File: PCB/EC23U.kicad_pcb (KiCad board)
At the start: 2 copper layers, 77.2 x 137.6 mm, 77 parts, among them J1 JST, SW1 BOOT0, SW10 EC_SW, SW11 EC_SW, SW12 EC_SW, SW13 EC_SW, SW14 EC_SW, SW15 EC_SW, SW16 EC_SW, SW17 EC_SW, SW18 EC_SW, SW19 EC_SW, SW2 EC_SW, SW20 EC_SW, SW21 EC_SW, SW22 EC_SW, SW23 EC_SW, SW24 EC_SW, SW25 EC_SW, SW26 EC_SW, SW27 EC_SW, SW28 EC_SW, SW3 EC_SW, SW4 EC_SW, SW5 EC_SW, SW6 EC_SW, SW7 EC_SW, SW8 EC_SW, SW9 EC_SW, U1 STM32F401CBUx, U2 XC6206PxxxMR, U3 74HC4051, U4 OPA350, Y1 8 MHz

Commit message: WIP
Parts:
- added J2: RGB, Connector_PinSocket_2.00mm:PinSocket_1x03_P2.00mm_Vertical, F.Cu at (140.5, 43.2)
- added U5: SN74AHCT1G125, Package_TO_SOT_SMD:SOT-23-5, B.Cu at (134.0, 43.9)
- moved Y1 51.5 mm to (109.9, 48.5), turned to 180 degrees
- moved C4 48.8 mm to (105.7, 44.4), turned to 90 degrees
- moved R6 48.5 mm to (107.0, 51.8)
- moved C1 48.5 mm to (100.0, 54.8)
- moved C7 48.5 mm to (104.6, 44.4)
- moved R8 48.5 mm to (101.1, 54.9)
- moved U1 48.5 mm to (101.8, 49.6)
- moved C6 48.5 mm to (96.6, 46.9)
- moved R3 48.5 mm to (96.6, 49.9)
- moved C5 48.5 mm to (98.9, 54.8)
- moved R7 48.2 mm to (103.1, 44.8), turned to 0 degrees
- moved SW1 47.8 mm to (99.1, 43.9), turned to -90 degrees
- moved C8 47.6 mm to (109.7, 51.2)
- moved C9 47.6 mm to (109.7, 52.3)
- moved R5 44.9 mm to (96.6, 53.0)
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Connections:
- D1 pad 2: D+ -> D-
- D1 pad 3: D- -> D+
- R1 pad 2: unconnected-(R1-Pad2) -> Net-(R1-Pad2)
- R2 pad 2: unconnected-(R2-Pad2) -> Net-(R2-Pad2)
- R4 pad 2: unconnected-(R4-Pad2) -> Net-(R4-Pad2)
- R5 pad 2: unconnected-(R5-Pad2) -> Net-(R5-Pad2)
- SW1 pad 1: VBAT -> BOOT0
- SW1 pad 2: BOOT0 -> VBAT
- U1 pad 10: ADC -> unconnected-(U1-Pad10)
- U1 pad 11: ADC -> unconnected-(U1-Pad11)
- U1 pad 13: ADC -> APLEX_OUT_PIN
- U1 pad 14: ADC -> unconnected-(U1-Pad14)
- U1 pad 15: ADC -> unconnected-(U1-Pad15)
- U1 pad 16: ADC -> unconnected-(U1-Pad16)
- U1 pad 17: ADC -> Net-(R4-Pad2)
- U1 pad 18: ADC -> Net-(R2-Pad2)
- U1 pad 19: ADC -> unconnected-(U1-Pad19)
- U1 pad 2: AMUX_SEL_2 -> AMUX_SEL_1
- U1 pad 25: unconnected-(U1-Pad25) -> Net-(R5-Pad2)
- U1 pad 26: unconnected-(U1-Pad26) -> Net-(R1-Pad2)
- U1 pad 3: AMUX_SEL_1 -> AMUX_SEL_0
- U1 pad 4: AMUX_SEL_0 -> APLEX_EN_PIN
- U1 pad 41: unconnected-(U1-Pad41) -> LED_3V3
- U1 pad 42: unconnected-(U1-Pad42) -> AMUX_SEL_2
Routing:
- net VBAT: track 18.4 -> 90.4 mm, vias 1 -> 6
- net +5V: track 7.38 -> 67.7 mm, vias 0 -> 2
- net LED_3V3: track 0.00 -> 41.5 mm, vias 0 -> 2
- net STROBE_0: track 187.4 -> 222.8 mm
- net STROBE_1: track 247.0 -> 277.8 mm, vias 13 -> 15
- net STROBE_3: track 189.4 -> 219.0 mm
- net STROBE_2: track 190.8 -> 219.7 mm
- net AMUX_SEL_2: track 6.51 -> 34.1 mm
- net APLEX_EN_PIN: track 0.00 -> 25.1 mm
- net AMUX_SEL_0: track 5.56 -> 29.9 mm
- net AMUX_SEL_1: track 5.96 -> 29.9 mm
- net APLEX_OUT_PIN: track 3.95 -> 22.7 mm
- net ADC: track 4.45 -> 17.7 mm
- net GND: track 11.5 -> 20.2 mm, vias 5 -> 16
- net D+: track 6.46 -> 14.2 mm, vias 0 -> 1
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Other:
- board text added: "+5V"
- board text added: "BOOT0"
- board text added: "Data"
- board text added: "GND"

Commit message: WIP PCB
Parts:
- added D2: LED, LED_THT:LED_D3.0mm, F.Cu at (106.1, 67.9)
- added G***: LOGO, LOGO, B.Cu at (161.4, 157.0)
- added G***: LOGO, LOGO, B.Cu at (126.8, 60.9)
- added G***: LOGO, cipulot_parts:Cipulot_all_info, B.Cu at (152.5, 82.6)
- added R18: 100, Resistor_SMD:R_0402_1005Metric, B.Cu at (120.6, 36.1)
- added SW4: EC_SW, cipulot_parts:ecs_pad_no_ring, F.Cu at (137.2, 49.0)
- J2: footprint Connector_PinSocket_2.00mm:PinSocket_1x03_P2.00mm_Vertical -> Connector_PinSocket_2.54mm:PinSocket_1x03_P2.54mm_Vertical
- moved R9 57.7 mm to (148.7, 135.5), turned to -90 degrees
- moved R14 52.2 mm to (121.6, 118.3), turned to 0 degrees
- moved H11 28.3 mm to (146.7, 161.3)
- moved H2 28.3 mm to (146.7, 49.0)
- moved H6 28.3 mm to (146.7, 110.9)
- moved H9 28.3 mm to (163.2, 60.9)
- moved SW5 28.3 mm to (156.2, 49.0)
- moved C1 28.3 mm to (124.0, 39.8)
- moved C13 28.3 mm to (90.7, 66.4)
- moved C2 28.3 mm to (113.8, 30.7)
- moved C3 28.3 mm to (118.9, 30.4)
- moved C5 28.3 mm to (122.9, 39.8)
- moved C7 28.3 mm to (128.6, 29.4)
- moved C8 28.3 mm to (133.7, 36.2)
- moved C9 28.3 mm to (133.7, 37.3)
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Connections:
- R10 pad 1: SENSE_4 -> SENSE_5
- R13 pad 1: SENSE_1 -> SENSE_0
- R14 pad 1: SENSE_0 -> SENSE_1
- R9 pad 1: SENSE_5 -> SENSE_4
- U1 pad 27: unconnected-(U1-Pad27) -> Num_Lock_Led
- U3 pad 1: SENSE_1 -> SENSE_0
- U3 pad 13: SENSE_5 -> SENSE_4
- U3 pad 14: SENSE_4 -> SENSE_5
- U3 pad 2: SENSE_0 -> SENSE_1
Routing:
- net SENSE_5: track 85.6 -> 223.1 mm
- net SENSE_4: track 67.3 -> 181.5 mm, vias 5 -> 7
- net SENSE_0: track 75.5 -> 138.5 mm, vias 4 -> 6
- net Net-(D2-Pad2): track 0.00 -> 61.4 mm, vias 0 -> 2
- net SENSE_1: track 75.0 -> 115.2 mm, vias 4 -> 6
- net SENSE_2: track 74.8 -> 96.8 mm
- net SENSE_3: track 101.5 -> 119.3 mm
- net GND: track 20.2 -> 25.6 mm, vias 16 -> 26
- net STROBE_3: track 219.0 -> 213.8 mm, vias 15 -> 14
- net STROBE_0: track 222.8 -> 224.7 mm
- net Num_Lock_Led: track 0.00 -> 1.40 mm
- net LED_5V: track 6.20 -> 7.45 mm
- net ADC: track 17.7 -> 16.7 mm
- net VBAT: track 90.4 -> 91.1 mm
- net +5V: track 67.7 -> 68.4 mm
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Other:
- board size 77.2 x 137.6 mm -> 77.1 x 137.6 mm
- board text added: "+"
- board text added: "-"

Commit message: Update PCB
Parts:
- C10: value 0.1u -> 100n
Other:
- board text added: "D+"
- board text added: "D-"
- board text added: "VBUS"

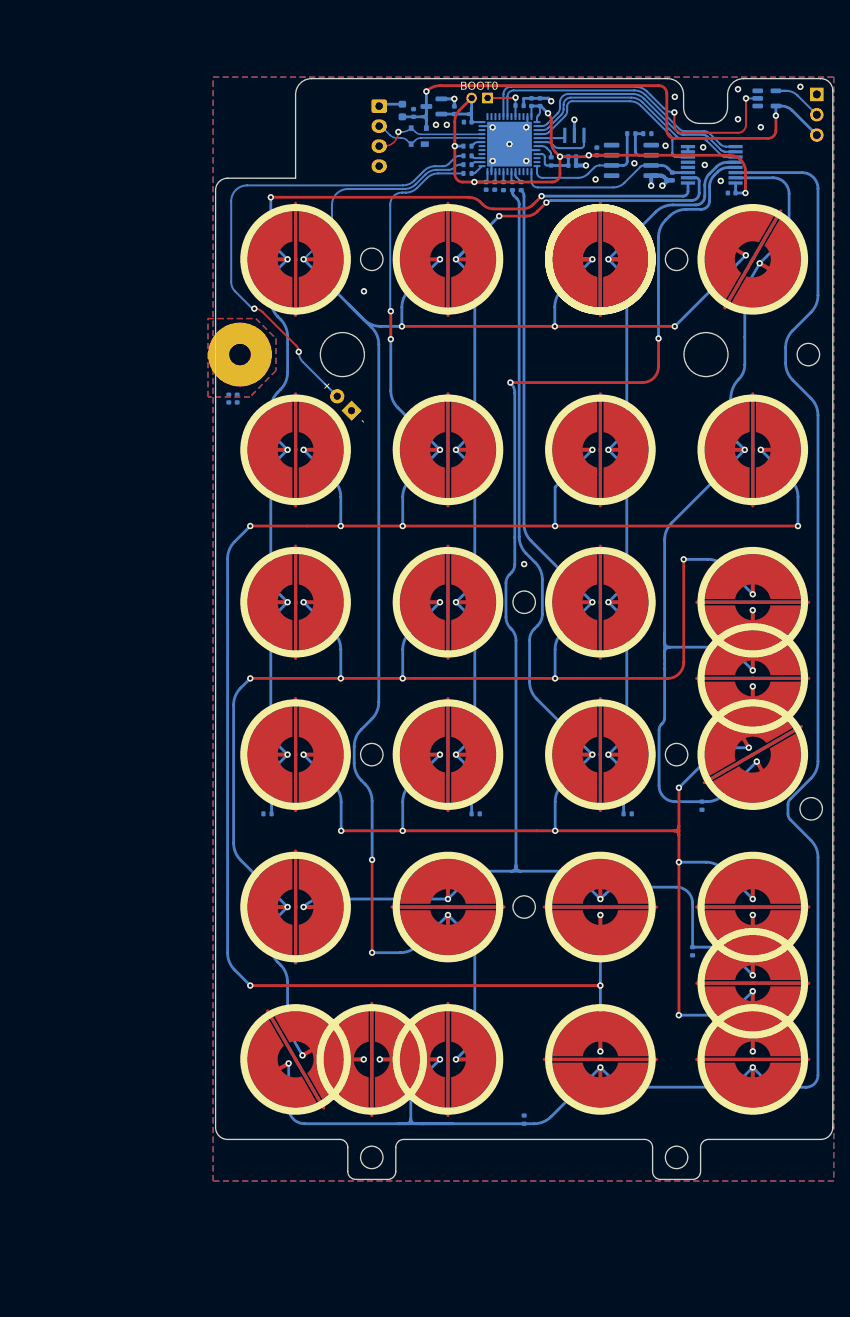
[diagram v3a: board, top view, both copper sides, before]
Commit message: Update for more GND stitching
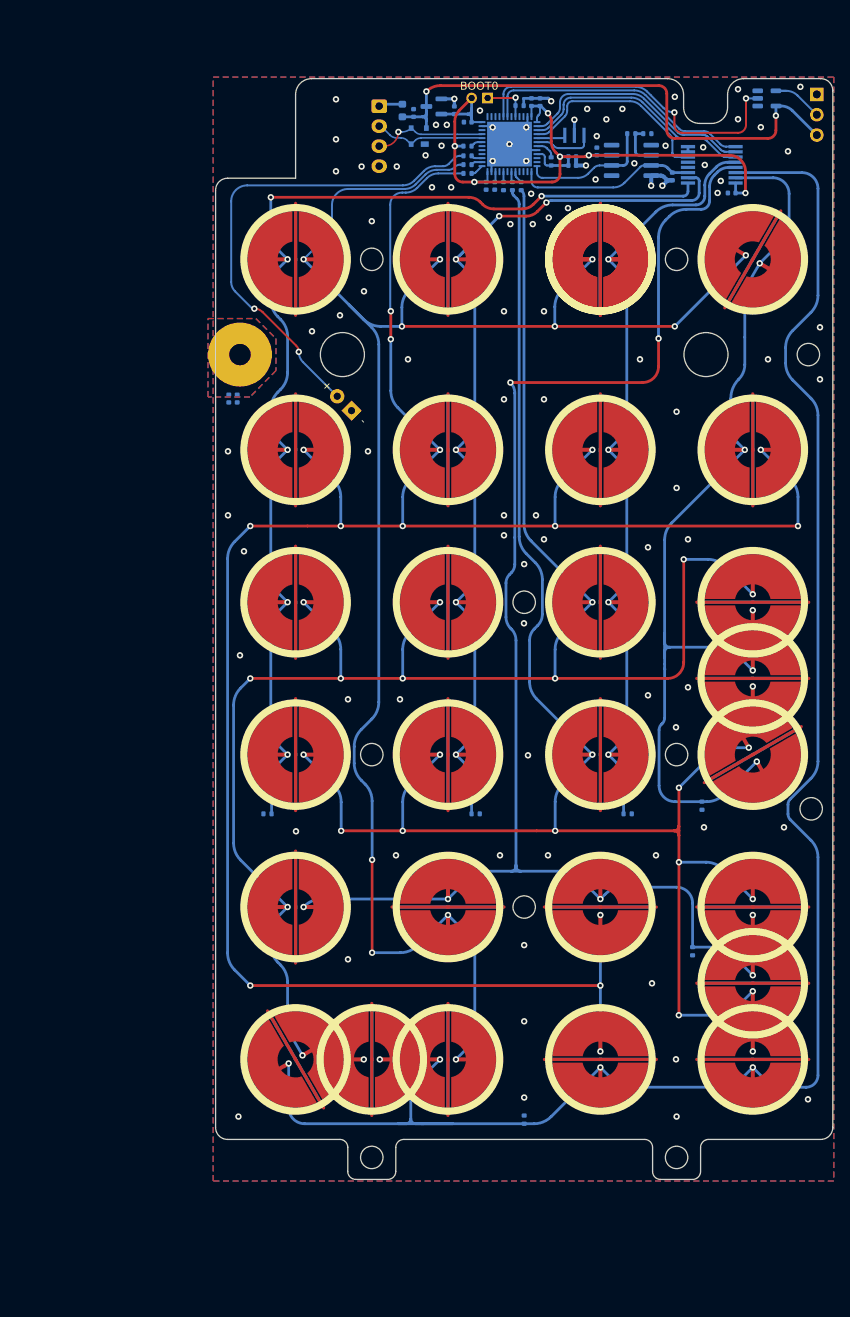
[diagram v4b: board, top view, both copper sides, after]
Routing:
- net GND: vias 26 -> 95

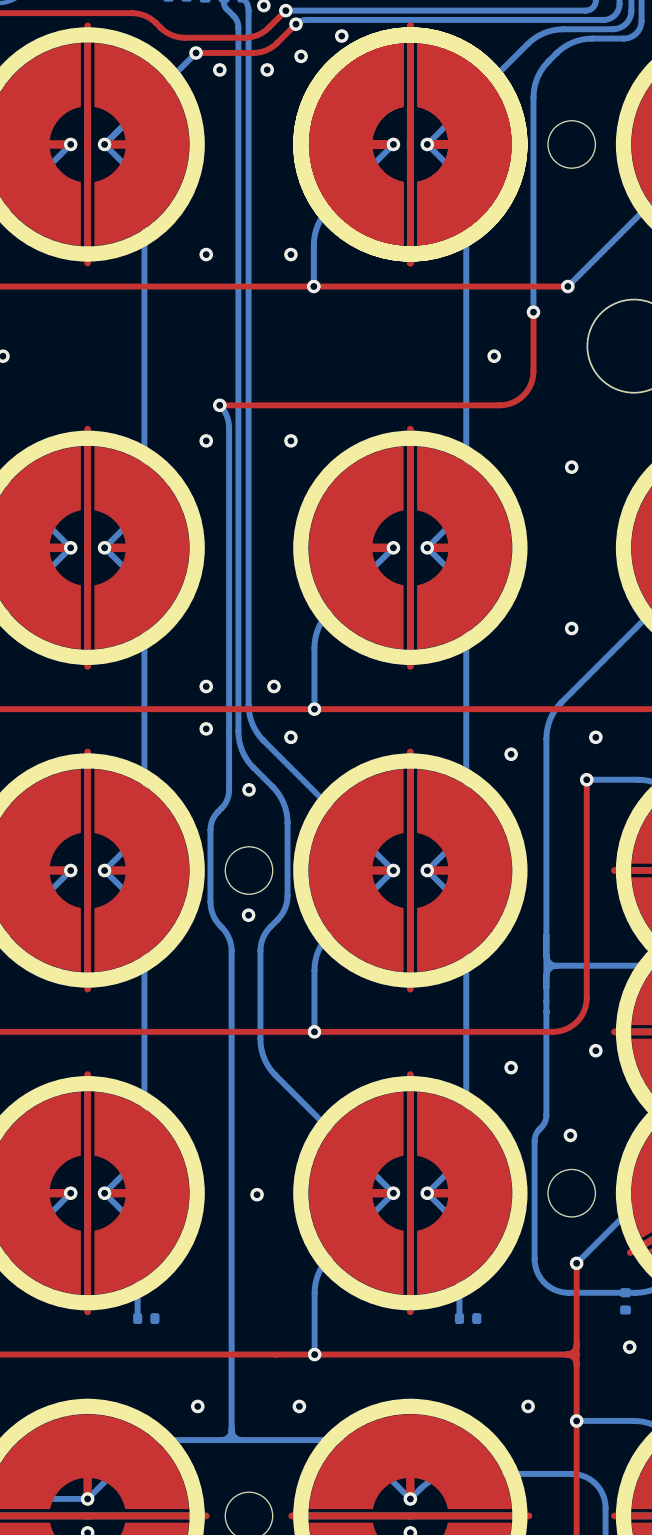
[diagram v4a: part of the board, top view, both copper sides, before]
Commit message: PCB cleanup of warnings
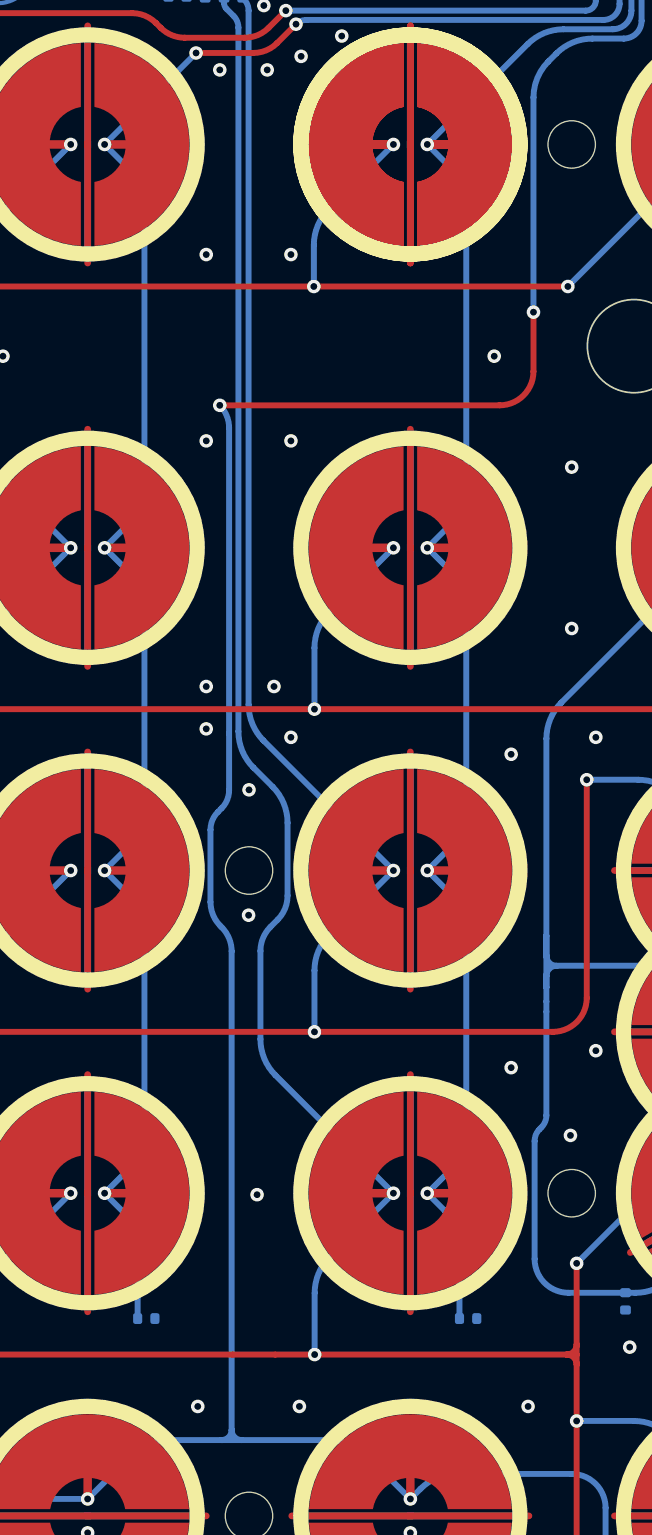
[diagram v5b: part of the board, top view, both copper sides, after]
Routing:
- net SENSE_1: track 115.2 -> 111.9 mm
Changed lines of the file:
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@@
   (segment (start 117.544723 157.06536) (end 118.140037 157.06536) (width 0.35) (layer "B.Cu") (net 23))
   (segment (start 162.3954 38.17487) (end 154.094423 38.17487) (width 0.35) (layer "B.Cu") (net 23))
-  (segment (start 113.4979 156.46536) (end 113.4979 156.46536) (width 0.35) (layer "B.Cu") (net 23))
   (segment (start 163.51672 121.63712) (end 160.938293 119.058693) (width 0.35) (layer "B.Cu") (net 23))
   (segment (start 98.22955 155.06536) (end 98.22955 149.528253) (width 0.35) (layer "B.Cu") (net 23))
@@
   (segment (start 100.21672 129.85698) (end 100.0954 129.9783) (width 0.35) (layer "B.Cu") (net 24))
   (segment (start 148.7204 134.99205) (end 151.491509 134.99205) (width 0.35) (layer "B.Cu") (net 24))
-  (segment (start 126.6454 124.7158) (end 126.6454 124.90205) (width 0.35) (layer "B.Cu") (net 24))
   (segment (start 154.094423 37.52463) (end 153.242815 37.52463) (width 0.35) (layer "B.Cu") (net 24))
   (segment (start 125.3954 89.479761) (end 125.3954 93.737373) (width 0.35) (layer "B.Cu") (net 24))
@@
   (segment (start 156.2454 100.4033) (end 153.84415 98.00205) (width 0.35) (layer "B.Cu") (net 25))
   (segment (start 152.637044 97.50205) (end 145.826708 97.50205) (width 0.35) (layer "B.Cu") (net 25))
-  (segment (start 145.265809 100.251841) (end 145.226708 100.212741) (width 0.35) (layer "B.Cu") (net 25))
-  (segment (start 145.826708 97.50205) (end 145.826708 97.50205) (width 0.35) (layer "B.Cu") (net 25))
   (segment (start 144.530074 114.808185) (end 144.530074 107.854972) (width 0.35) (layer "B.Cu") (net 25))
   (segment (start 150.488677 116.808185) (end 149.900285 116.808185) (width 0.35) (layer "B.Cu") (net 25))
@@
   (segment (start 121.4979 76.423441) (end 121.4979 88.283159) (width 0.35) (layer "B.Cu") (net 27))
   (segment (start 119.1454 72.8283) (end 120.619221 71.354479) (width 0.35) (layer "B.Cu") (net 27))
-  (segment (start 119.1454 49.0158) (end 121.4979 46.6633) (width 0.35) (layer "B.Cu") (net 27))
   (segment (start 121.4979 69.233159) (end 121.4979 52.610941) (width 0.35) (layer "B.Cu") (net 27))
   (segment (start 149.145073 38.82511) (end 148.145743 38.82511) (width 0.35) (layer "B.Cu") (net 27))
@@
   (segment (start 161.203687 30.437837) (end 164.2479 33.48205) (width 0.35) (layer "B.Cu") (net 51))
   (segment (start 113.8454 31.2033) (end 114.9454 31.2033) (width 0.35) (layer "B.Cu") (net 51))
-  (segment (start 114.9454 31.2033) (end 114.9454 31.2033) (width 0.35) (layer "B.Cu") (net 51))
   (segment (start 159.1354 29.85205) (end 159.1354 31.06455) (width 0.35) (layer "B.Cu") (net 51))
   (segment (start 115.4454 31.7033) (end 115.4454 31.7158) (width 0.35) (layer "B.Cu") (net 51))
